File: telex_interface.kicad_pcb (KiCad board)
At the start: 4 copper layers, 63.5 x 34.5 mm, 58 parts, among them J1 DB25_Female_MountingHoles, J2 Conn_02x20_Odd_Even, J3 Conn_01x03_Male, J4 Conn_02x04_Odd_Even, U1 max3387, U2 74LVC1G08

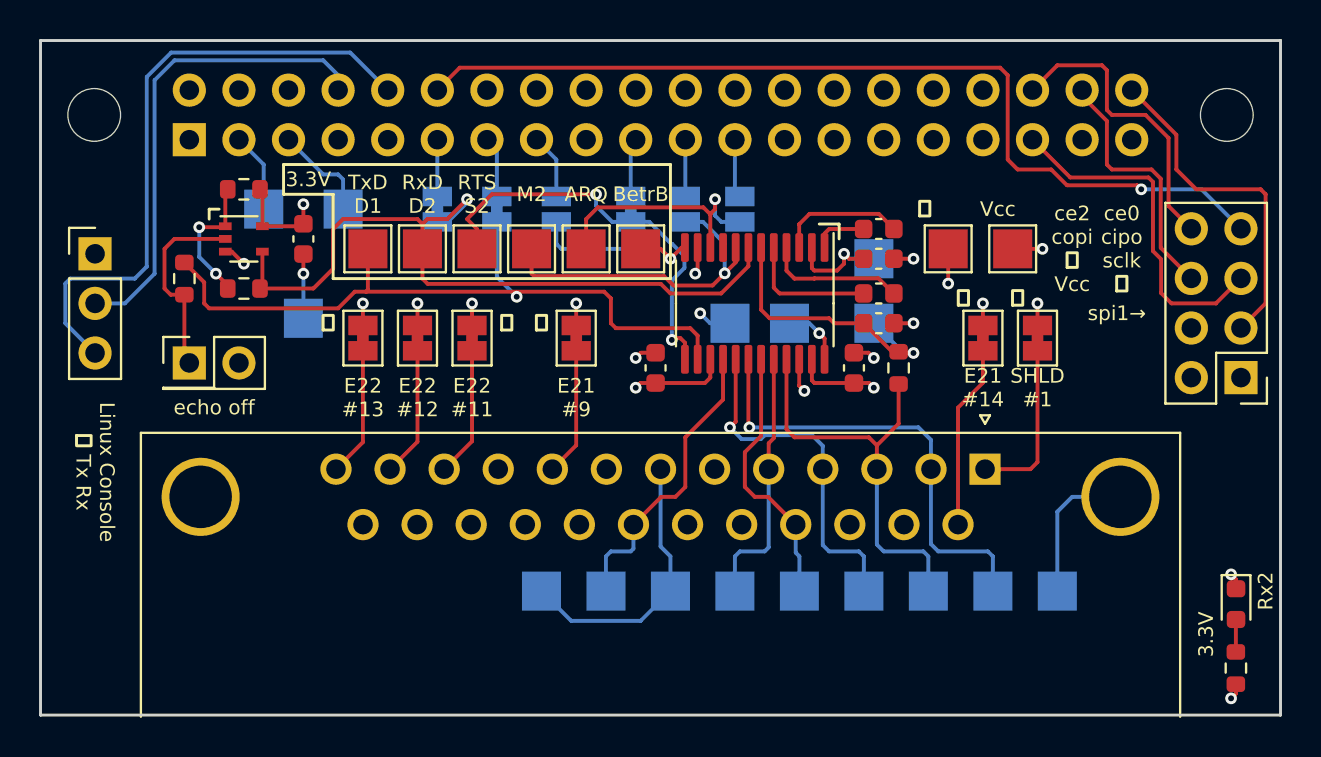
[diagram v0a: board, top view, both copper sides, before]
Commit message: Changes needed for kicad 5.99 - 6.99
Fix alignment issue in schematic.
Newly introduced warning about silkscreen width/text height:
 - change design rules to match what was already successfully produced

Because of rounding issues (I guess, moving traces by 1 pixel or so
makes DRC pass) I turned off "soldermask aperture over traces with
different nets".
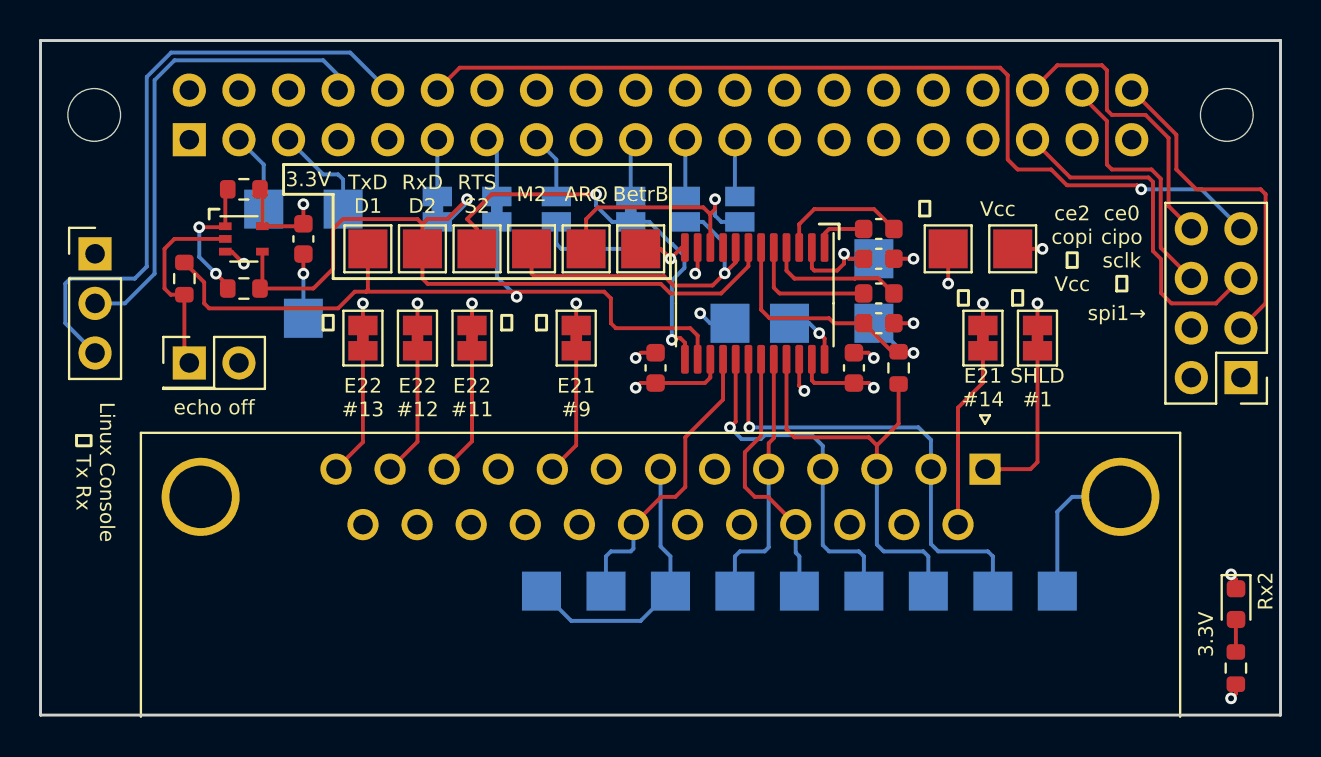
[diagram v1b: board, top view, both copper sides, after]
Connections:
- net /GPIO14_Cons_Tx renamed /GPIO14/Cons/Tx
- net /GPIO15_Cons_Rx renamed /GPIO15/Cons/Rx
- net /GPIO16_CE2 renamed /GPIO16/CE2
- net /GPIO18_CE0 renamed /GPIO18/CE0
- net /GPIO19_CIPO renamed /GPIO19/CIPO
- net /GPIO20_COPI renamed /GPIO20/COPI
- net /GPIO21_SCLK renamed /GPIO21/SCLK
- net /GPIO2_SDA renamed /GPIO2/SDA
- net /GPIO3_SCL renamed /GPIO3/SCL
- net /RxD_PC renamed /RxD/PC
- net /RxD_TTY renamed /RxD/TTY
- net /V10_E21@14 renamed /V10/E21@14
- net /V10_E21@9 renamed /V10/E21@9
- net /V10_E22@11 renamed /V10/E22@11
- net /V10_E22@12 renamed /V10/E22@12
- net /V10_E22@13 renamed /V10/E22@13
- net /~{BetrB_DTR} renamed /~{BetrB/DTR}
- net /~{S2_RTS} renamed /~{S2/RTS}
- net V10_ARQ renamed V10/ARQ
- net V10_BetrB_DTR renamed V10/BetrB/DTR
- net V10_D1_TxD renamed V10/D1/TxD
- net V10_D2_RxD renamed V10/D2/RxD
- net V10_M2 renamed V10/M2
- net V10_S2_RTS renamed V10/S2/RTS

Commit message: Fix mistakes made during first spin of board (RevA):
R1 Pulldown to -6V was on RxD (input of TTY, output of maxim driver)
instead of TxD (output of TTY, input of maxim driver).
  ==> moved to V10/D1/TxD signal, Pin 2 of DSUB

Raspi GPIO17 was on net RxD/TTY (output of the single gate buffer U2)
instead of net RxD/PC (input to U2), so both outputs (raspi & U2) were
on the same net.
  ==> connected GPIO17 to net RxD/PC

Silkscreen: RxD/TxD labels were swapped near JP8/JP9 on the bottom
of the PCB, adding even more confusion ;).
  ==> Fixed silkscreen labels.
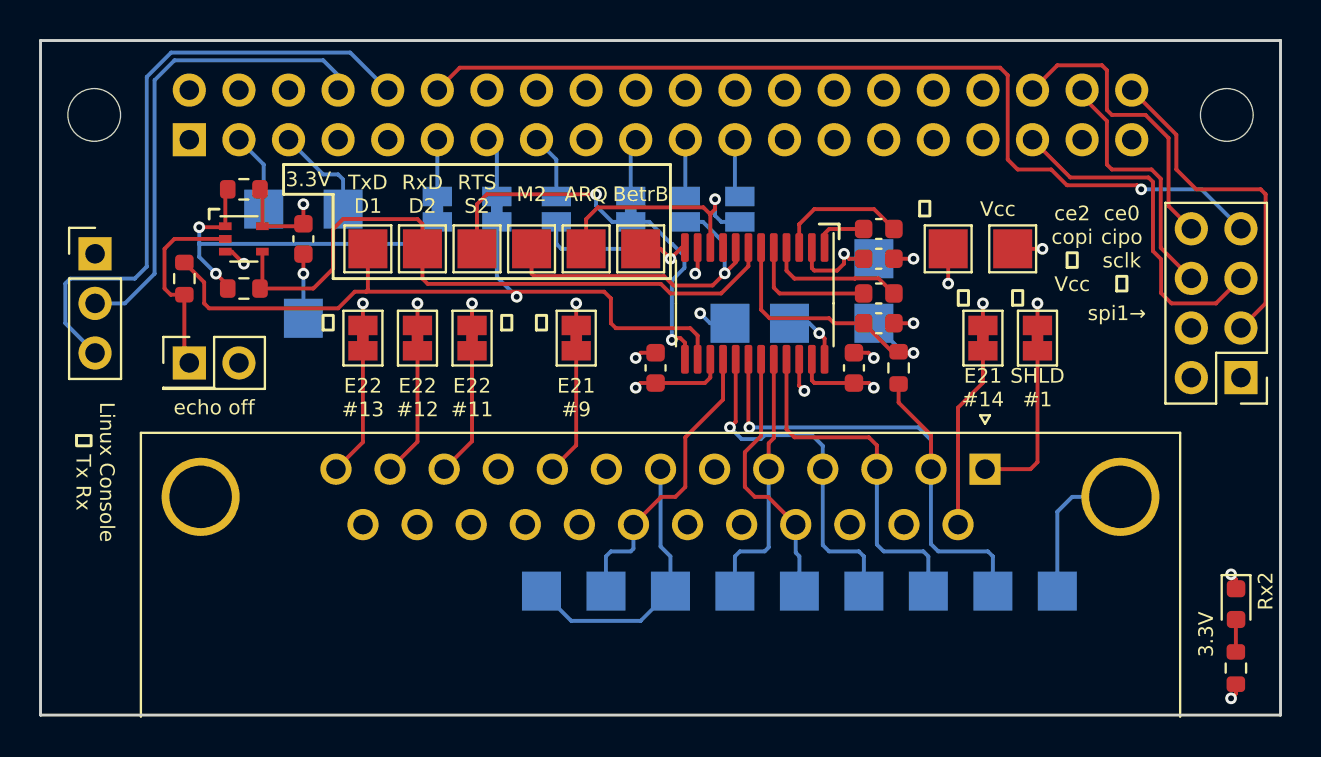
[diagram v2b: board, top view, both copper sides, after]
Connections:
- JP8 pad 1: /RxD/TTY -> /RxD/PC
- R1 pad 1: V10/D2/RxD -> V10/D1/TxD
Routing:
- net /RxD/PC: track 6.64 -> 19.8 mm
- net V10/D1/TxD: track 23.6 -> 28.7 mm
- net /RxD/TTY: track 38.6 -> 34.2 mm, vias 1 -> 0
- net V10/D2/RxD: track 21.9 -> 18.3 mm
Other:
- board text added: "IO17 D2 TxD"
- board text added: "IO27 D1 TxD"
- board text added: "github.com:vogelchr/telex_interface Rev.B"
- board text removed: "IO17 D1 TxD"
- board text removed: "IO27 D2 RxD"
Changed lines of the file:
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@@
       (stroke (width 0.1) (type solid)) (layer "F.Fab"))
     (pad "1" smd roundrect (at -0.825 0 90) (size 0.8 0.95) (layers "F.Cu" "F.Paste" "F.Mask") (roundrect_rratio 0.25)
-      (net 10 "V10{slash}D2{slash}RxD") (pintype "passive"))
+      (net 8 "V10{slash}D1{slash}TxD") (pintype "passive"))
     (pad "2" smd roundrect (at 0.825 0 90) (size 0.8 0.95) (layers "F.Cu" "F.Paste" "F.Mask") (roundrect_rratio 0.25)
       (net 3 "-6V") (pintype "passive"))
@@
       (stroke (width 0.05) (type solid)) (layer "B.CrtYd"))
     (pad "1" smd rect (at -0.65 0 90) (size 1 1.5) (layers "B.Cu" "B.Mask")
-      (net 65 "/RxD{slash}TTY") (pinfunction "A") (pintype "passive"))
+      (net 71 "/RxD{slash}PC") (pinfunction "A") (pintype "passive"))
     (pad "2" smd rect (at 0.65 0 90) (size 1 1.5) (layers "B.Cu" "B.Mask")
       (net 43 "/GPIO17") (pinfunction "B") (pintype "passive"))
@@
     (effects (font (size 0.75 0.75) (thickness 0.1)) (justify mirror))
   )
-  (gr_text "IO17\nD1\nTxD" (at 165.1 108.712) (layer "B.SilkS")
+  (gr_text "IO17\nD2\nTxD" (at 165.1 108.712) (layer "B.SilkS")
     (effects (font (size 0.75 0.75) (thickness 0.1)) (justify mirror))
   )
@@
     (effects (font (size 0.75 0.75) (thickness 0.1)) (justify mirror))
   )
-  (gr_text "IO27\nD2\nRxD" (at 168.148 108.712) (layer "B.SilkS")
+  (gr_text "IO27\nD1\nTxD" (at 168.148 108.712) (layer "B.SilkS")
     (effects (font (size 0.75 0.75) (thickness 0.1)) (justify mirror))
   )
@@
   (gr_text "IO11\nARQ" (at 180.594 108.204) (layer "B.SilkS")
     (effects (font (size 0.75 0.75) (thickness 0.1)) (justify mirror))
+  )
+  (gr_text "github.com:vogelchr/telex_interface Rev.B" (at 161.798 129.794) (layer "B.SilkS")
+    (effects (font (size 1 1) (thickness 0.15)) (justify mirror))
   )
   (gr_text "IO22\nBetr" (at 171.196 108.204) (layer "B.SilkS")
@@
   (segment (start 170.434 124.714) (end 171.958 126.238) (width 0.2) (layer "B.Cu") (net 6))
   (segment (start 196.85 124.714) (end 196.85 120.65) (width 0.2) (layer "B.Cu") (net 6))
+  (segment (start 188.722 115.062) (end 190.38 116.72) (width 0.2) (layer "F.Cu") (net 8))
+  (segment (start 190.38 116.72) (end 190.38 118.469669) (width 0.2) (layer "F.Cu") (net 8))
   (segment (start 181.031 112.8445) (end 181.031 116.2815) (width 0.2) (layer "F.Cu") (net 8))
+  (segment (start 188.722 114.109) (end 188.722 115.062) (width 0.2) (layer "F.Cu") (net 8))
   (segment (start 181.031 116.2815) (end 181.0815 116.332) (width 0.2) (layer "F.Cu") (net 8))
   (via (at 181.0815 116.332) (size 0.6) (drill 0.3) (layers "F.Cu" "B.Cu") (net 8))
@@
   (segment (start 187.198 116.84) (end 187.61 117.252) (width 0.2) (layer "F.Cu") (net 10))
   (segment (start 183.388 116.84) (end 187.198 116.84) (width 0.2) (layer "F.Cu") (net 10))
-  (segment (start 188.722 116.14) (end 187.61 117.252) (width 0.2) (layer "F.Cu") (net 10))
   (segment (start 187.61 117.252) (end 187.61 118.469669) (width 0.2) (layer "F.Cu") (net 10))
-  (segment (start 188.722 114.109) (end 188.722 116.14) (width 0.2) (layer "F.Cu") (net 10))
   (segment (start 182.981 112.8445) (end 182.981 116.433) (width 0.2) (layer "F.Cu") (net 10))
   (segment (start 187.61 122.332) (end 187.96 122.682) (width 0.2) (layer "B.Cu") (net 10))
@@
   (segment (start 156.019 109.22) (end 158.75 109.22) (width 0.2) (layer "F.Cu") (net 65))
   (segment (start 160.274 105.664) (end 164.084 105.664) (width 0.2) (layer "F.Cu") (net 65))
-  (segment (start 165.608 105.664) (end 164.592 105.664) (width 0.2) (layer "F.Cu") (net 65))
   (segment (start 176.546969 108.982969) (end 164.608969 108.982969) (width 0.2) (layer "F.Cu") (net 65))
   (segment (start 179.635006 109.474) (end 177.038 109.474) (width 0.2) (layer "F.Cu") (net 65))
@@
   (segment (start 159.766 108.204) (end 159.766 106.172) (width 0.2) (layer "F.Cu") (net 65))
   (segment (start 181.031 108.078006) (end 179.635006 109.474) (width 0.2) (layer "F.Cu") (net 65))
-  (segment (start 166.624 104.648) (end 165.608 105.664) (width 0.2) (layer "F.Cu") (net 65))
   (segment (start 158.75 109.22) (end 159.766 108.204) (width 0.2) (layer "F.Cu") (net 65))
   (segment (start 164.608969 108.982969) (end 164.338 108.712) (width 0.2) (layer "F.Cu") (net 65))
   (segment (start 164.084 105.664) (end 164.338 105.918) (width 0.2) (layer "F.Cu") (net 65))
-  (segment (start 164.592 105.664) (end 164.338 105.918) (width 0.2) (layer "F.Cu") (net 65))
   (segment (start 164.338 105.918) (end 164.338 107.188) (width 0.2) (layer "F.Cu") (net 65))
   (segment (start 159.766 106.172) (end 160.274 105.664) (width 0.2) (layer "F.Cu") (net 65))
   (segment (start 177.038 109.474) (end 176.546969 108.982969) (width 0.2) (layer "F.Cu") (net 65))
   (segment (start 164.338 108.712) (end 164.338 107.188) (width 0.2) (layer "F.Cu") (net 65))
-  (via (at 166.624 104.648) (size 0.6) (drill 0.3) (layers "F.Cu" "B.Cu") (net 65))
-  (segment (start 166.624 104.816162) (end 166.624 104.648) (width 0.2) (layer "B.Cu") (net 65))
-  (segment (start 165.634162 105.806) (end 166.624 104.816162) (width 0.2) (layer "B.Cu") (net 65))
-  (segment (start 167.132 106.172) (end 166.624 105.664) (width 0.2) (layer "F.Cu") (net 66))
-  (segment (start 167.894 104.394) (end 166.624 105.664) (width 0.2) (layer "F.Cu") (net 66))
+  (segment (start 173.228 104.394) (end 167.64 104.394) (width 0.2) (layer "F.Cu") (net 66))
   (segment (start 177.199862 111.76) (end 177.108362 111.8515) (width 0.2) (layer "F.Cu") (net 66))
+  (segment (start 167.132 104.902) (end 167.132 107.188) (width 0.2) (layer "F.Cu") (net 66))
   (segment (start 177.781 111.995) (end 177.546 111.76) (width 0.2) (layer "F.Cu") (net 66))
-  (segment (start 173.228 104.394) (end 167.894 104.394) (width 0.2) (layer "F.Cu") (net 66))
-  (segment (start 167.132 107.188) (end 167.132 106.172) (width 0.2) (layer "F.Cu") (net 66))
   (segment (start 177.781 112.8445) (end 177.781 111.995) (width 0.2) (layer "F.Cu") (net 66))
+  (segment (start 167.64 104.394) (end 167.132 104.902) (width 0.2) (layer "F.Cu") (net 66))
   (segment (start 177.546 111.76) (end 177.199862 111.76) (width 0.2) (layer "F.Cu") (net 66))
   (via (at 173.228 104.394) (size 0.6) (drill 0.3) (layers "F.Cu" "B.Cu") (net 66))
@@
   (via (at 153.7615 108.458) (size 0.6) (drill 0.3) (layers "F.Cu" "B.Cu") (net 71))
   (via (at 152.908 106.0805) (size 0.6) (drill 0.3) (layers "F.Cu" "B.Cu") (net 71))
+  (segment (start 165.1 105.806) (end 165.1 106.68) (width 0.2) (layer "B.Cu") (net 71))
   (segment (start 153.7615 108.458) (end 152.908 107.6045) (width 0.2) (layer "B.Cu") (net 71))
-  (segment (start 152.908 107.6045) (end 152.908 106.0805) (width 0.2) (layer "B.Cu") (net 71))
+  (segment (start 165.1 106.68) (end 164.846 106.934) (width 0.2) (layer "B.Cu") (net 71))
+  (segment (start 152.908 107.6045) (end 152.908 106.934) (width 0.2) (layer "B.Cu") (net 71))
+  (segment (start 152.908 106.934) (end 152.908 106.0805) (width 0.2) (layer "B.Cu") (net 71))
+  (segment (start 164.846 106.934) (end 152.908 106.934) (width 0.2) (layer "B.Cu") (net 71))
   (zone (net 6) (net_name "GND") (layer "In1.Cu") (hatch edge 0.508)
     (connect_pads (clearance 0.3))
